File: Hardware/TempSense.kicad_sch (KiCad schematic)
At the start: 29 parts, among them J1 USB_B_Micro, Q1 SS8050-G, Q2 SS8050-G, U1 ESP32-WROOM-32, U2 AMS1117-3.3, U3 CP2102N-Axx-xQFN28, U4 HDC1080

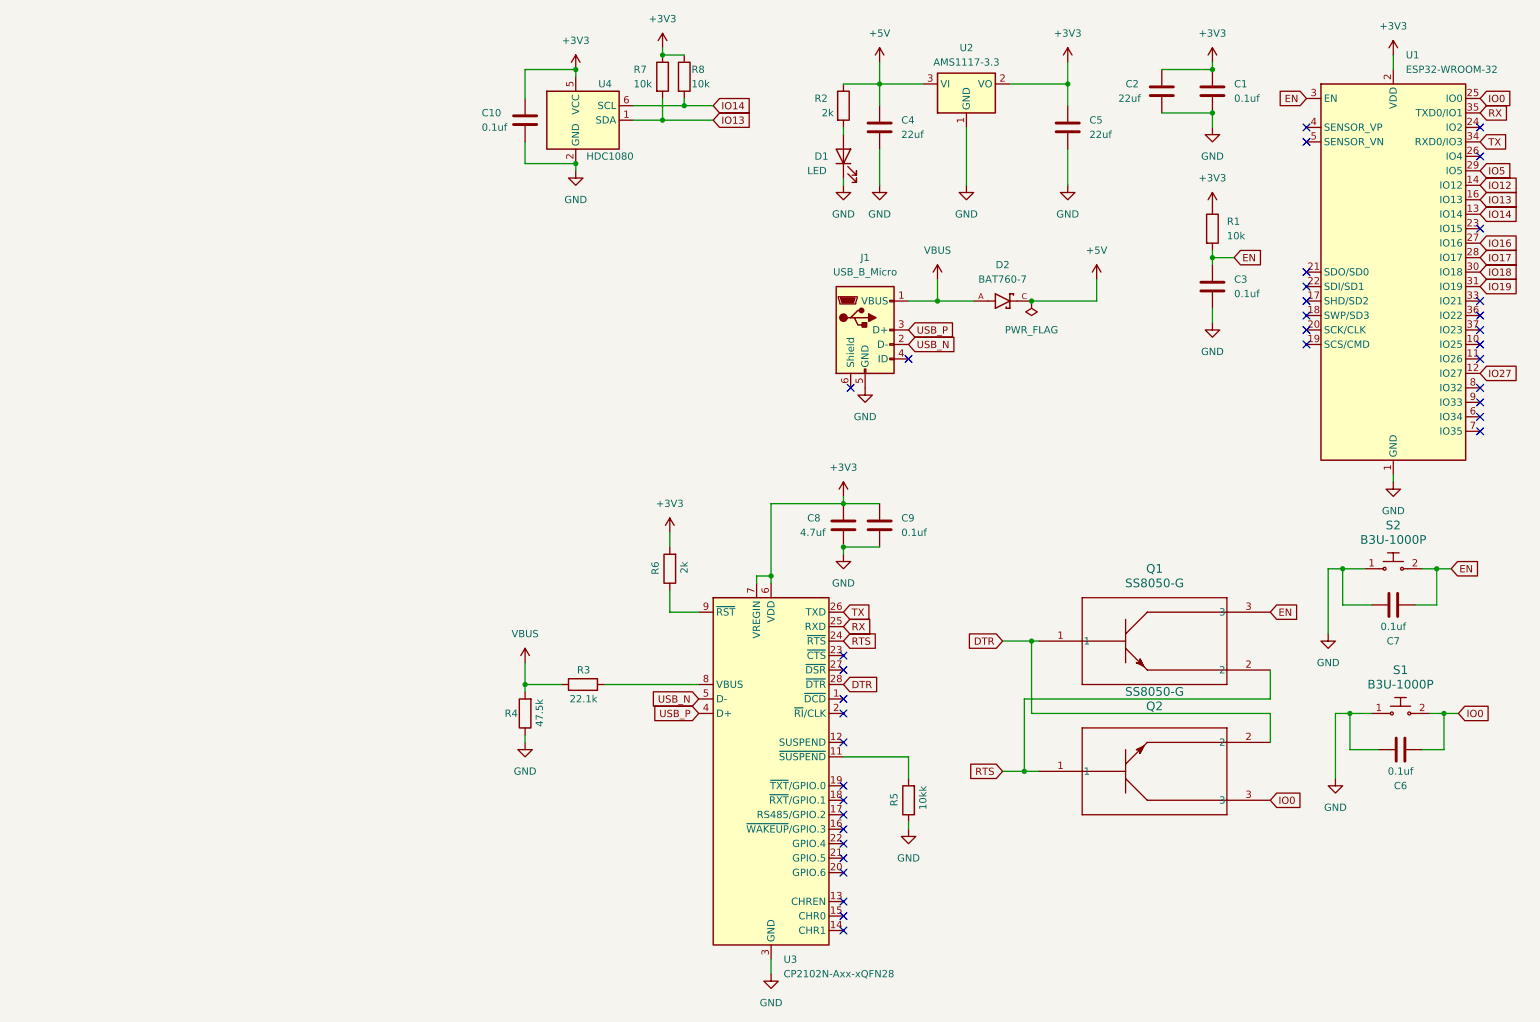
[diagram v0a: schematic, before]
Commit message: Added labels to shematic and produced pdf version
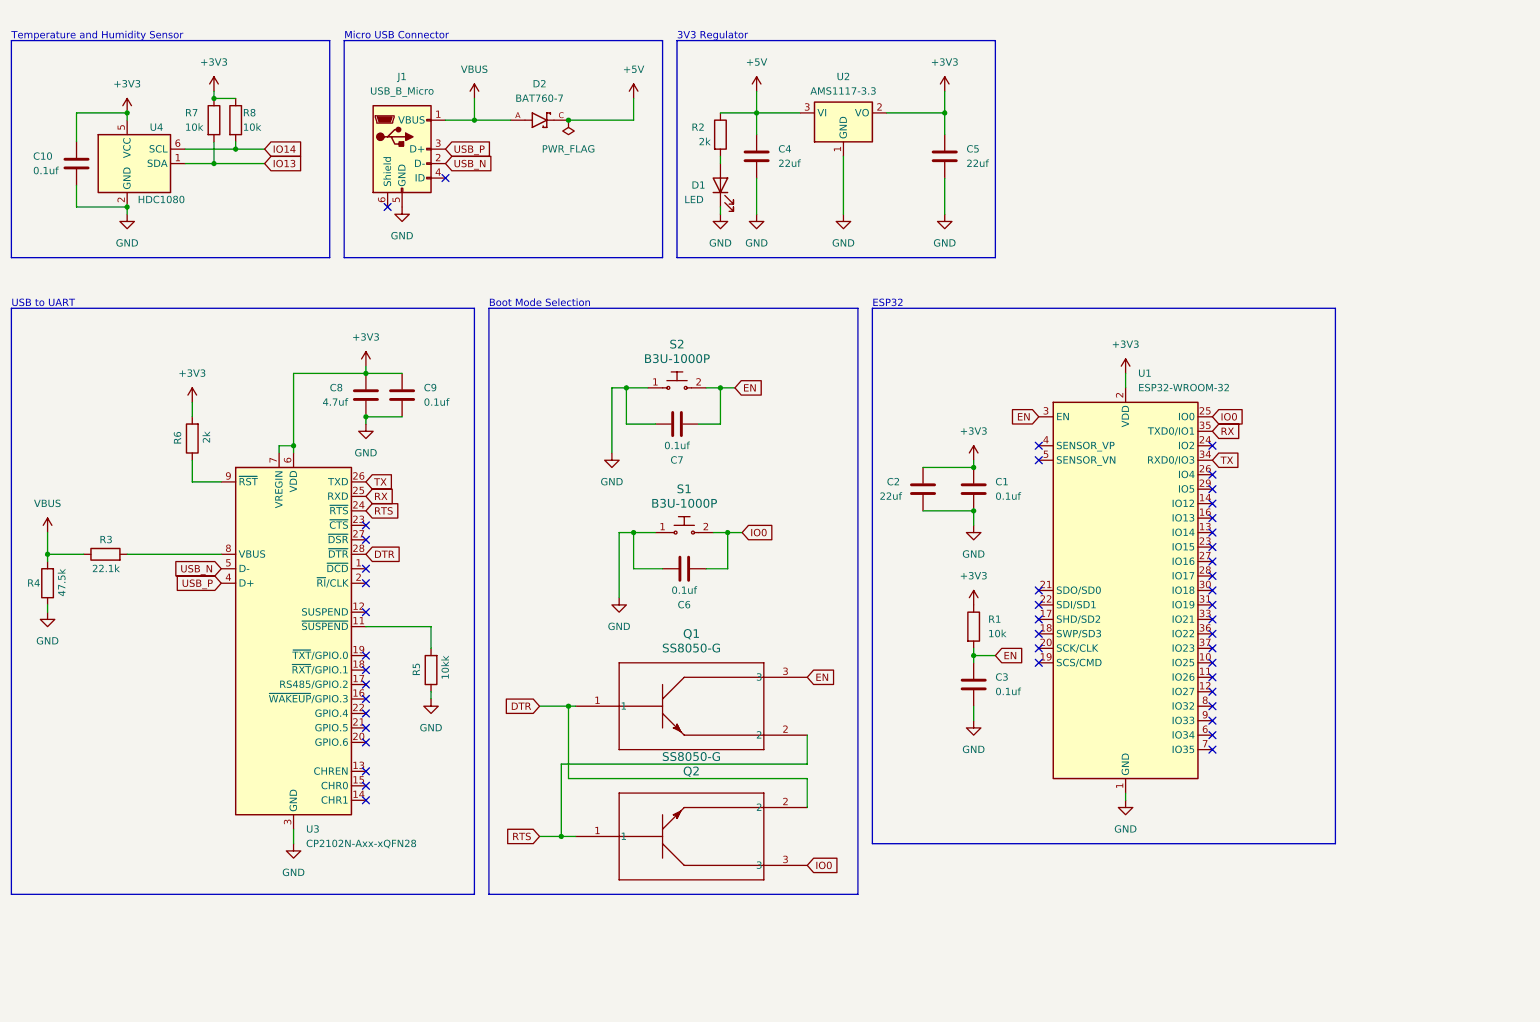
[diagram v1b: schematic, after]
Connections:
- net IO13: no longer U1.16 (IO13)
- net IO14: no longer U1.13 (IO14)
- net IO12: no longer names the net of U1.14 (IO12)
- net IO16: no longer names the net of U1.27 (IO16)
- net IO17: no longer names the net of U1.28 (IO17)
- net IO18: no longer names the net of U1.30 (IO18)
- net IO19: no longer names the net of U1.31 (IO19)
- net IO27: no longer names the net of U1.12 (IO27)
- net IO5: no longer names the net of U1.29 (IO5)
- no-connect marks 37 -> 46
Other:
- note added: "3V3 Regulator"
- note added: "Boot Mode Selection"
- note added: "ESP32"
- note added: "Micro USB Connector"
- note added: "Temperature and Humidity Sensor"
- note added: "USB to UART"
- moved on the sheet: C1, C10, C2, C3, C4, C5, C6, C7, C8, C9, D1, D2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
